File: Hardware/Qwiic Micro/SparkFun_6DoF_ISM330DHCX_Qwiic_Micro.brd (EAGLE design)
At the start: 17.8 x 12.7 mm, 37 parts, among them J1 Qwiic Right Angle, U1 ISM330DHCX

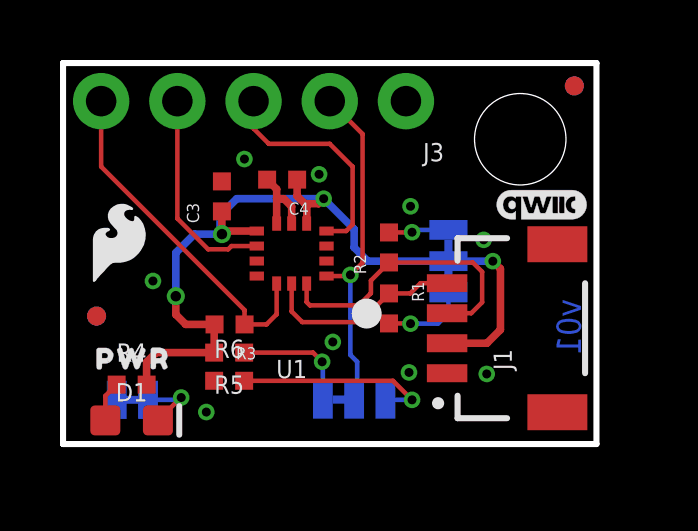
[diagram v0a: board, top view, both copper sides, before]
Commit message: Updates labels on Qwiic Micro, Updates IC on Qwiic Micro and Micro
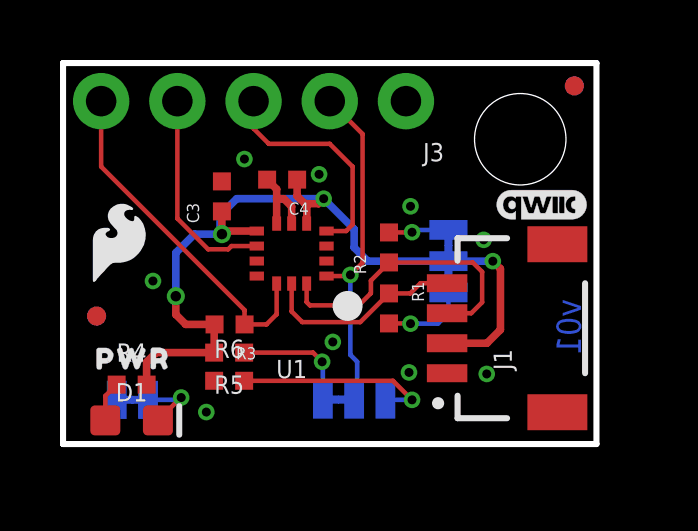
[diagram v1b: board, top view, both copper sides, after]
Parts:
- removed U$39: (no value), ISMTopMini:SDO2113
- added U$3: (no value), ISMTopMini:POCI2114
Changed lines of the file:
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@@
 </element>
 <element name="U$38" library="ISMTopMini" package="#CS#2114" value="" x="1.27" y="9.3472" smashed="yes" rot="MR90"/>
-<element name="U$39" library="ISMTopMini" package="SDO2113" value="" x="8.89" y="8.9916" smashed="yes" rot="MR90"/>
 <element name="U$42" library="ISMTopMini" package="GND4" value="" x="11.4808" y="9.1948" smashed="yes" rot="MR90"/>
 <element name="U$44" library="ISMTopMini" package="INT110" value="" x="6.2992" y="9.0932" smashed="yes" rot="MR90"/>
@@
 <element name="LOGO1" library="SparkFun-Aesthetics" package="QWIIC_3MM" value="QWIIC_LOGO_3MM" x="15.9512" y="7.9756" smashed="yes"/>
 <element name="LOGO3" library="SparkFun-Aesthetics" package="BLANK" value="SFE_LOGO_NAME_FLAMEBLANK" x="-39.37" y="-15.24" smashed="yes"/>
+<element name="U$3" library="ISMTopMini" package="POCI2114" value="" x="8.89" y="8.89" smashed="yes" rot="MR90"/>
 </elements>
 <signals>

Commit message: Resizes and reroutes the Qwiic Micro board
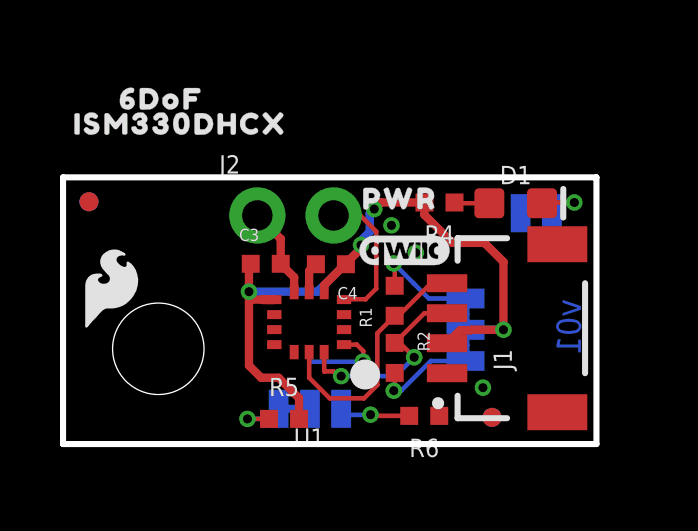
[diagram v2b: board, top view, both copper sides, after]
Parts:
- removed J3: (no value), SparkFun-Connectors:1X05_NO_SILK
- removed R3: 10k, SparkFun-Resistors:0402-TIGHT
- removed U$3: (no value), ISMTopMini:POCI2114
- removed U$38: (no value), ISMTopMini:#CS#2114
- removed U$45: (no value), ISMTopMini:INT2111
- added J2: (no value), SparkFun-Connectors:1X02_NO_SILK
- moved LED 14.8 mm to (15.8, 7.70)
- moved D1 14.7 mm to (15.1, 8.03)
- moved STANDOFF1 13.9 mm to (3.17, 3.17)
- moved U$16 13.8 mm to (15.8, 6.12)
- moved R4 11.9 mm to (12.5, 8.05), turned to 180 degrees
- moved FD1 11.4 mm to (14.3, 0.89)
- moved FID1 11.4 mm to (14.3, 0.89)
- moved U$28 10.4 mm to (11.2, 8.18)
- moved R6 6.61 mm to (12.0, 0.94), turned to 180 degrees
- moved LOGO1 4.82 mm to (11.4, 6.45)
- moved U$2 4.64 mm to (3.28, 11.5), flipped to the top
- moved U$1 4.57 mm to (3.91, 10.7), flipped to the top
- moved LOGO2 4.47 mm to (15.8, -2.23)
- moved FD2 3.82 mm to (0.86, 8.08)
- moved FID2 3.82 mm to (0.86, 8.08)
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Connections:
- net SDA/PICO renamed SDA
- removed net !CS!: J3.5, R3.1, U1.P12
- removed net INT2: J3.4, U1.P9
- removed net POCI/SA0: ADDR.2, J3.2, U1.P1
- new net SA0: ADDR.2, U1.P1
- net 3.3V: no longer R3.2
- net GND: now also J2.1; no longer J3.1
- net INT1: now also J2.2; no longer J3.3
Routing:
- net !CS!: track 11.7 -> 0.00 mm
- net POCI/SA0: track 11.5 -> 0.00 mm, vias 1 -> 0
- net INT2: track 7.03 -> 0.00 mm
- net N$7: track 6.75 -> 2.71 mm
- net 3.3V: track 29.1 -> 26.2 mm
- net SA0: track 0.00 -> 2.87 mm, vias 0 -> 1
- net INT1: track 7.63 -> 4.77 mm
- net SDA: track 9.82 -> 6.97 mm, vias 0 -> 2
- net N$1: track 4.00 -> 1.90 mm
- net SCL: track 6.80 -> 8.34 mm
- net N$6: track 2.02 -> 3.41 mm
- net GND: track 2.77 -> 4.09 mm, vias 9 -> 3
- net N$5: track 2.82 -> 3.64 mm
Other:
- board size 17.8 x 12.7 mm -> 17.8 x 8.9 mm

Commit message: Extends board to 0.75", adds better labels, adds 0402 LED to design
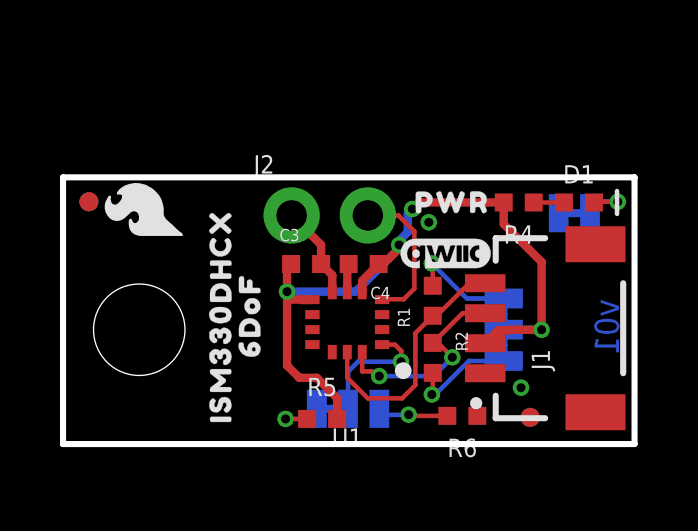
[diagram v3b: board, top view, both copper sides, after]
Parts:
- removed U$13: (no value), bot:#0X6A#11
- removed U$42: (no value), ISMTopMini:GND4
- removed U$44: (no value), ISMTopMini:INT110
- added U$3: (no value), ISMTopMini:#0X6A#2117
- added U$4: (no value), ISMTopMini:#INT1#112
- added U$5: (no value), ISMTopMini:#GND#5
- added U$7: (no value), ISMTopMini:X2114
- added U$8: (no value), ISMTopMini:Y2115
- added U$9: (no value), ISMTopMini:Z2116
- D1: device SparkFun-LED:LED-0603 -> ISM330DHCX:0402-TIGHT
- moved U$2 7.79 mm to (6.22, 4.29), turned to 90 degrees
- moved U$1 6.54 mm to (5.26, 4.27), turned to 90 degrees
- moved LOGO2 3.79 mm to (17.3, 1.25)
- moved U$14 3.65 mm to (6.15, 1.24), turned to 0 degrees
- moved U$29 2.80 mm to (2.67, 7.80), turned to 90 degrees
- moved R4 2.64 mm to (15.2, 8.05)
- moved D1 2.11 mm to (17.2, 8.05)
- moved U$25 1.92 mm to (16.2, 3.81)
- moved U$28 1.76 mm to (13.0, 8.05)
- moved LOGO1 1.38 mm to (12.8, 6.35)
- moved C3 1.35 mm to (8.10, 6.00)
- moved ADDR 1.27 mm to (9.50, 1.17)
- moved FD1 1.27 mm to (15.6, 0.89)
- moved FID1 1.27 mm to (15.6, 0.89)
- moved I2C_PU 1.27 mm to (14.7, 3.81)
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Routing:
- net SA0: track 2.87 -> 4.23 mm
- net GND: track 4.09 -> 4.07 mm, vias 3 -> 2
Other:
- board size 17.8 x 8.9 mm -> 19.1 x 8.9 mm

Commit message: Moves resistor so that PWR silk is close to the LED
* Fixes some trace bends
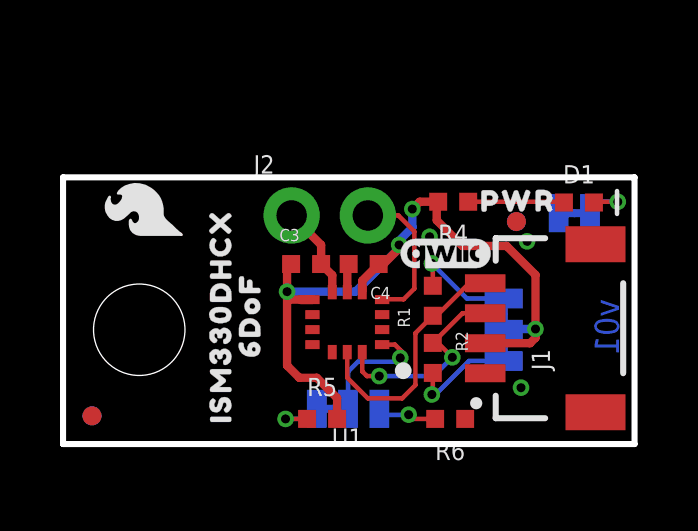
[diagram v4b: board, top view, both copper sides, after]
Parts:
- moved FD2 7.14 mm to (0.97, 0.94)
- moved FID2 7.14 mm to (0.97, 0.94)
- moved FD1 6.54 mm to (15.1, 7.42)
- moved FID1 6.54 mm to (15.1, 7.42)
- moved U$28 2.18 mm to (15.2, 8.10)
- moved R4 2.18 mm to (13.0, 8.08)
- moved R6 0.42 mm to (12.9, 0.84)
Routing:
- net N$2: track 1.01 -> 3.20 mm
- net 3.3V: track 26.5 -> 25.8 mm
- net GND: vias 2 -> 3

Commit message: small adjustments
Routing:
- net GND: vias 3 -> 4
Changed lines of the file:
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@@
 <setting verticaltext="up"/>
 </settings>
-<grid distance="0.05" unitdist="inch" unit="inch" style="dots" multiple="1" display="yes" altdistance="0.001" altunitdist="inch" altunit="inch"/>
+<grid distance="0.05" unitdist="inch" unit="inch" style="dots" multiple="1" display="yes" altdistance="0.005" altunitdist="inch" altunit="inch"/>
 <layers>
 <layer number="1" name="Top" color="4" fill="1" visible="yes" active="yes"/>
@@
 <layer number="45" name="Holes" color="7" fill="1" visible="yes" active="yes"/>
 <layer number="46" name="Milling" color="3" fill="1" visible="no" active="yes"/>
-<layer number="47" name="Measures" color="7" fill="1" visible="yes" active="yes"/>
-<layer number="48" name="Document" color="7" fill="1" visible="yes" active="yes"/>
+<layer number="47" name="Measures" color="7" fill="1" visible="no" active="yes"/>
+<layer number="48" name="Document" color="7" fill="1" visible="no" active="yes"/>
 <layer number="49" name="Reference" color="13" fill="1" visible="yes" active="yes"/>
 <layer number="50" name="dxf" color="7" fill="1" visible="no" active="no"/>
@@
 <via x="15.4686" y="6.7564" extent="1-16" drill="0.3"/>
 <via x="12.2174" y="6.9088" extent="1-16" drill="0.3"/>
+<via x="13.1064" y="1.6256" extent="1-16" drill="0.3"/>
 </signal>
 <signal name="SCL">
@@
 <wire x1="13.5396" y1="5.3608" x2="12.454" y2="4.2752" width="0.1524" layer="1"/>
 <wire x1="12.454" y1="4.2752" x2="12.32535" y2="4.2752" width="0.1524" layer="1"/>
-<wire x1="9.4742" y1="3.064" x2="9.4742" y2="2.2098" width="0.1524" layer="1"/>
-<wire x1="9.4742" y1="2.2098" x2="10.16" y2="1.524" width="0.1524" layer="1"/>
+<wire x1="9.4742" y1="3.064" x2="9.4742" y2="1.9558" width="0.1524" layer="1"/>
+<wire x1="9.4742" y1="1.9558" x2="9.906" y2="1.524" width="0.1524" layer="1"/>
 <wire x1="11.74595" y1="3.6958" x2="12.32535" y2="4.2752" width="0.1524" layer="1"/>
-<wire x1="10.16" y1="1.524" x2="11.303" y2="1.524" width="0.1524" layer="1"/>
+<wire x1="9.906" y1="1.524" x2="11.303" y2="1.524" width="0.1524" layer="1"/>
 <wire x1="11.303" y1="1.524" x2="11.74595" y2="1.96695" width="0.1524" layer="1"/>
 <wire x1="11.74595" y1="1.96695" x2="11.74595" y2="3.6958" width="0.1524" layer="1"/>
@@
 <wire x1="9.9742" y1="2.421" x2="9.9742" y2="3.064" width="0.1524" layer="1"/>
 <via x="10.541" y="2.26455" extent="1-16" drill="0.3"/>
-<wire x1="12.32535" y1="3.3702" x2="12.49669375" y2="3.3702" width="0.1524" layer="1"/>
-<wire x1="12.49669375" y1="3.3702" x2="12.975346875" y2="2.891546875" width="0.1524" layer="1"/>
+<wire x1="12.467346875" y1="2.891546875" x2="12.32535" y2="3.03354375" width="0.1524" layer="1"/>
+<wire x1="12.32535" y1="3.3702" x2="12.32535" y2="3.03354375" width="0.1524" layer="1"/>
+<wire x1="12.467346875" y1="2.891546875" x2="12.975346875" y2="2.891546875" width="0.1524" layer="1"/>
 <via x="12.975346875" y="2.891546875" extent="1-16" drill="0.3"/>
-<wire x1="12.975346875" y1="2.891546875" x2="12.34835" y2="2.26455" width="0.1524" layer="16"/>
-<wire x1="12.34835" y1="2.26455" x2="10.541" y2="2.26455" width="0.1524" layer="16"/>
+<wire x1="12.975346875" y1="2.891546875" x2="12.086346875" y2="2.891546875" width="0.1524" layer="16"/>
+<wire x1="12.086346875" y1="2.891546875" x2="11.45935" y2="2.26455" width="0.1524" layer="16"/>
+<wire x1="11.45935" y1="2.26455" x2="10.541" y2="2.26455" width="0.1524" layer="16"/>
 <wire x1="10.541" y1="2.26455" x2="10.13065" y2="2.26455" width="0.1524" layer="1"/>
 <wire x1="10.13065" y1="2.26455" x2="9.9742" y2="2.421" width="0.1524" layer="1"/>
